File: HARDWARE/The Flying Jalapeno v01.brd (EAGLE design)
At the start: 73.7 x 72.4 mm, 95 parts, among them J2 7V, Q1 16MHZ, Q3 P-Channel MOSFET, Q6 200mA/50V, Q7 200mA/50V, U4 ATMEGA2560AU

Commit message: Added labels to 2x30 connector
also a lot of other small stuff as I went through the checklist
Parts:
- removed IC3: (no value), SparkFun-PowerIC:SOT223
- removed JP6: FLYING_JALAPENO_V2FEMALE, SparkFun:FLYING_JALAPENO_V2_F
- added JP4: 2x30 RA FEMALE HEADER, Testing:FLYING_JALAPENO_V2_F
- added LOGO2: SFE_LOGO_FLAME.3_INCH, SparkFun-Aesthetics:SFE_LOGO_FLAME_.3
- added U1: ATMEGA2560AU, SparkFun-DigitalIC:TQFP100
- JP3: value AVR_SPI_PRG_6PTH -> (none)
- Q2, Q4: value (none) -> MMBT2222A
- Q3: value P-Channel MOSFET -> NDP6020P
- Q5: value (none) -> NDP6020P
- Q6, Q7: value 200mA/50V -> BSS138, 200mA/50V
- U2, U3: value (none) -> LM1117
- U4: value ATMEGA2560AU -> LM1117; device SparkFun:TQFP100 -> SparkFun-PowerIC:SOT223
- moved U4 38.4 mm to (16.5, 50.4), turned to 90 degrees
- moved R13 0.28 mm to (8.14, 12.6)
- moved R9 0.25 mm to (7.94, 14.1)
- renumbered IC1 to U2, IC2 to U3, J2 to JP1, JP15 to JP2, Q1 to Y1, SJ5 to SJ3, SJ6 to SJ4
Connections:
- net 31/CAPRETURN2: now also U1.59; no longer U4.59
- net 33/V1_3.3V: now also U1.57; no longer U4.57
- net 34/RAW_PASS_LED: now also U1.56; no longer U4.56
- net 35/V1_5V: now also U1.55; no longer U4.55
- net 36/V2_3.3V: now also U1.54; no longer U4.54
- net 37/V2_3.7V: now also U1.53; no longer U4.53
- net 38/V2_4.2V: now also U1.50; no longer U4.50
- net 39/V2_5V: now also U1.70; no longer U4.70
- net 40/FAIL: now also U1.52; no longer U4.52
- net 41/PASS: now also U1.51; no longer U4.51
- net 42/PT_FAIL: now also U1.42; no longer U4.42
- net 43/PT_PASS: now also U1.41; no longer U4.41
- net 44/PT_CTRL: now also U1.40; no longer U4.40
- net 45/CAPSENSE1: now also JP4.5, U1.39; no longer JP6.5, U4.39
- net 46/CAPSENSE2: now also JP4.58, U1.38; no longer JP6.58, U4.38
- net 47/CAPRETURN1: now also U1.37; no longer U4.37
- net 48/PWR_CTRL1: now also U1.36; no longer U4.36
- net 49/PWR_CTRL2: now also U1.35; no longer U4.35
- net A0: now also JP4.37, U1.97; no longer JP6.37, U4.97
- net A1: now also JP4.8, U1.96; no longer JP6.8, U4.96
- net A10: now also JP4.42, U1.87; no longer JP6.42, U4.87
- net A11: now also JP4.13, U1.86; no longer JP6.13, U4.86
- net A12: now also JP4.43, U1.85; no longer JP6.43, U4.85
- net A13/RAW_READ: now also U1.84; no longer U4.84
- net A14/PT_READ_V1: now also U1.83; no longer U4.83
- net A15/PT_READ_V2: now also U1.82; no longer U4.82
- net A2: now also JP4.38, U1.95; no longer JP6.38, U4.95
- net A3: now also JP4.9, U1.94; no longer JP6.9, U4.94
- net A4: now also JP4.39, U1.93; no longer JP6.39, U4.93
- net A5: now also JP4.10, U1.92; no longer JP6.10, U4.92
- net A6: now also JP4.40, U1.91; no longer JP6.40, U4.91
- net A7: now also JP4.11, U1.90; no longer JP6.11, U4.90
- net A8: now also JP4.41, U1.89; no longer JP6.41, U4.89
- net A9: now also JP4.12, U1.88; no longer JP6.12, U4.88
- net AREF: now also U1.98; no longer U4.98
- net D10: now also JP4.18, U1.23; no longer JP6.18, U4.23
- net D11: now also JP4.48, U1.24; no longer JP6.48, U4.24
- net D12: now also JP4.19, U1.25; no longer JP6.19, U4.25
- net D13: now also JP4.49, U1.26; no longer JP6.49, U4.26
- net D2: now also JP4.14, U1.6; no longer JP6.14, U4.6
- net D22: now also JP4.24, U1.78; no longer JP6.24, U4.78
- net D23: now also JP4.54, U1.77; no longer JP6.54, U4.77
- net D24: now also JP4.25, U1.76; no longer JP6.25, U4.76
- net D25: now also JP4.55, U1.75; no longer JP6.55, U4.75
- net D26: now also JP4.26, U1.74; no longer JP6.26, U4.74
- net D27: now also JP4.56, U1.73; no longer JP6.56, U4.73
- net D28: now also JP4.27, U1.72; no longer JP6.27, U4.72
- net D29: now also JP4.57, U1.71; no longer JP6.57, U4.71
- net D3: now also JP4.44, U1.7; no longer JP6.44, U4.7
- net D30: now also JP4.28, U1.60; no longer JP6.28, U4.60
- net D4: now also JP4.15, U1.1; no longer JP6.15, U4.1
- net D5: now also JP4.45, U1.5; no longer JP6.45, U4.5
- net D6: now also JP4.16, U1.15; no longer JP6.16, U4.15
- net D7: now also JP4.46, U1.16; no longer JP6.46, U4.16
- net D8: now also JP4.17, U1.17; no longer JP6.17, U4.17
- net D9: now also JP4.47, U1.18; no longer JP6.47, U4.18
- net GND: now also JP4.1, JP4.31, U1.11, U1.32, U1.62, U1.81, U1.99; no longer JP6.1, JP6.31, U4.11, U4.32, U4.62, U4.81, U4.99
- net N$10: now also U4.1; no longer IC3.1
- net N$19: now also JP4.6; no longer JP6.6
- net N$20: now also JP4.35; no longer JP6.35
- net N$6: now also JP4.7; no longer JP6.7
- net N$7: now also JP4.36; no longer JP6.36
- net N$73: now also U1.33; no longer U4.33
- net N$74: now also U1.34; no longer U4.34
- net PB0: now also JP4.60, U1.19; no longer JP6.60, U4.19
- net PB1: now also JP4.30, U1.20; no longer JP6.30, U4.20
- net PB2: now also JP4.59, U1.21; no longer JP6.59, U4.21
- net PB3: now also JP4.29, U1.22; no longer JP6.29, U4.22
- net PC5: now also U1.58; no longer U4.58
- net RAW: now also JP4.34, JP4.4, U4.3; no longer IC3.3, JP6.34, JP6.4
- net RESET: now also U1.30; no longer U4.30
- net RX0: now also U1.2; no longer U4.2
- net RX1: now also JP4.52, U1.45; no longer JP6.52, U4.45
- net RX2: now also JP4.51, U1.12; no longer JP6.51, U4.12
- net RX3: now also JP4.50, U1.63; no longer JP6.50, U4.63
- net SCL: now also JP4.53, U1.43; no longer JP6.53, U4.43
- net SDA: now also JP4.23, U1.44; no longer JP6.23, U4.44
- net TX0: now also U1.3; no longer U4.3
- net TX1: now also JP4.22, U1.46; no longer JP6.22, U4.46
- net TX2: now also JP4.21, U1.13; no longer JP6.21, U4.13
- net TX3: now also JP4.20, U1.64; no longer JP6.20, U4.64
- net V1: now also JP4.2, JP4.32; no longer JP6.2, JP6.32
- net V2: now also JP4.3, JP4.33; no longer JP6.3, JP6.33
- net VCC: now also U1.10, U1.100, U1.31, U1.61, U1.80; no longer U4.10, U4.100, U4.31, U4.61, U4.80
- net VREG2OUT: now also U4.2, U4.4; no longer IC3.2, IC3.4
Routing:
- net N$23: track 21.4 -> 22.5 mm
- net 48/PWR_CTRL1: track 53.6 -> 54.6 mm
- net N$22: track 21.4 -> 22.5 mm
- net FTDI_VCC: track 36.7 -> 37.5 mm
- net VCC: track 187.5 -> 187.0 mm
- net 49/PWR_CTRL2: track 37.9 -> 38.5 mm
- net 44/PT_CTRL: track 82.5 -> 83.0 mm
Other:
- board text added: "A0"
- board text added: "A1"
- board text added: "A10"
- board text added: "A11"
- board text added: "A12"
- board text added: "A2"
- board text added: "A3"
- board text added: "A4"
- board text added: "A5"
- board text added: "A6"
- board text added: "A7"
- board text added: "A8"
- board text added: "A9"
- board text added: "CS1"
- board text added: "CS2"
- board text added: "D10"
- board text added: "D11"
- board text added: "D12"
- board text added: "D13"
- board text added: "D2"
- board text added: "D22"
- board text added: "D23"
- board text added: "D24"
- board text added: "D25"
- board text added: "D26"
- board text added: "D27"
- board text added: "D28"
- board text added: "D29"
- board text added: "D3"
- board text added: "D30"
- board text added: "D4"
- board text added: "D5"
- board text added: "D50"
- board text added: "D51"
- board text added: "D52"
- board text added: "D53"
- board text added: "D6"
- board text added: "D7"
- board text added: "D8"
- board text added: "D9"
- board text added: "FAIL"
- board text added: "GND"
- board text added: "GNd"
- board text added: "PASS"
- board text added: "PT"
- board text added: "Rx1"
- board text added: "Rx2"
- board text added: "Rx3"
- board text added: "SCL"
- board text added: "SDA"
- board text added: "Tx1"
- board text added: "Tx2"
- board text added: "Tx3"

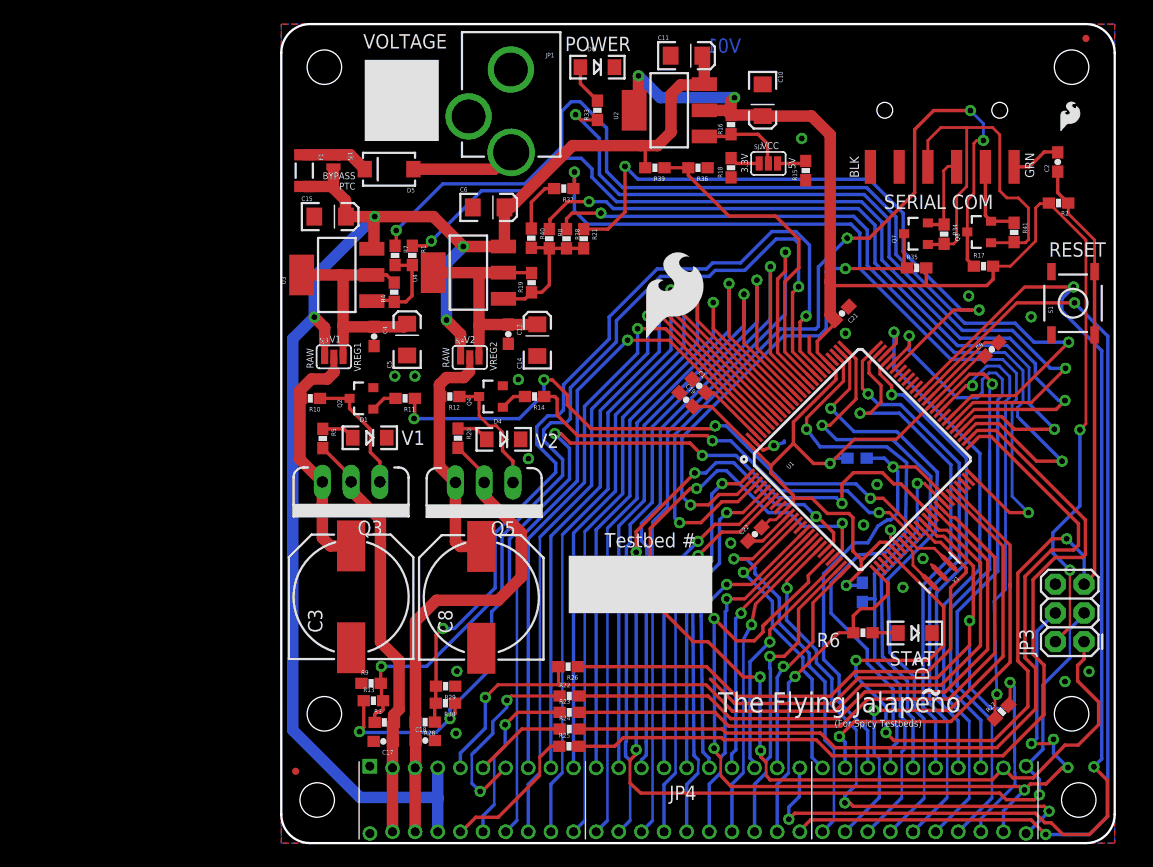
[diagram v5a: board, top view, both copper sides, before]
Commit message: added labels to all parts
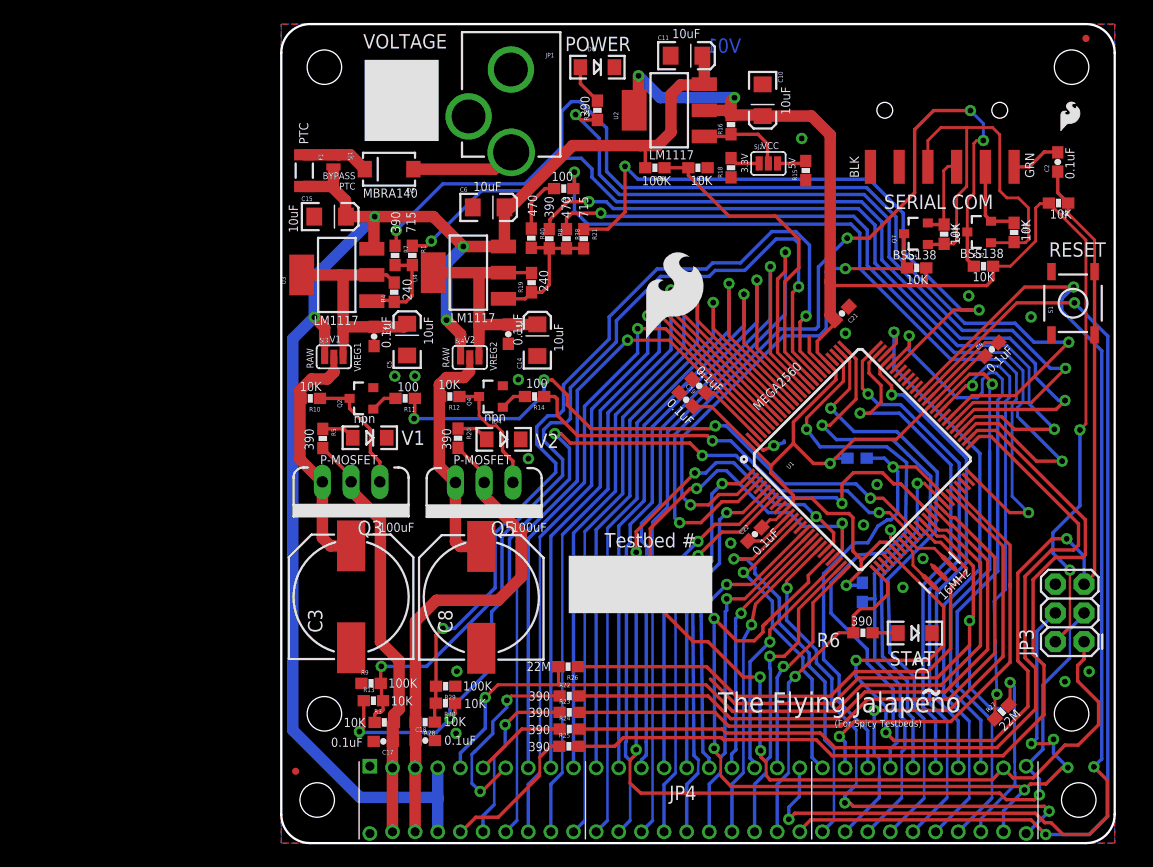
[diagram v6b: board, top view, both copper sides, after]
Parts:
- moved LOGO1 14.0 mm to (67.0, 40.5)
- moved LOGO4 12.8 mm to (44.5, 59.7)
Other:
- board text added: "0.1uF"
- board text added: "100"
- board text added: "100K"
- board text added: "100uF"
- board text added: "10K"
- board text added: "10uF"
- board text added: "16MHz"
- board text added: "22M"
- board text added: "240"
- board text added: "390"
- board text added: "470"
- board text added: "715"
- board text added: "BSS138"
- board text added: "LM1117"
- board text added: "MBRA140"
- board text added: "MEGA2560"
- board text added: "Optional I2C pullups"
- board text added: "P-MOSFET"
- board text added: "PTC"
- board text added: "npn"
